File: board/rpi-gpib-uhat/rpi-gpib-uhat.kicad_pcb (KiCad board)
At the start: 2 copper layers, 65 x 30 mm, 44 parts, among them J1 RPI_GPIO, J2 GPIB, U1 SN75160BDW, U2 SN75162BDW, U3 LM317_SOT-223, U4 CAT24C32

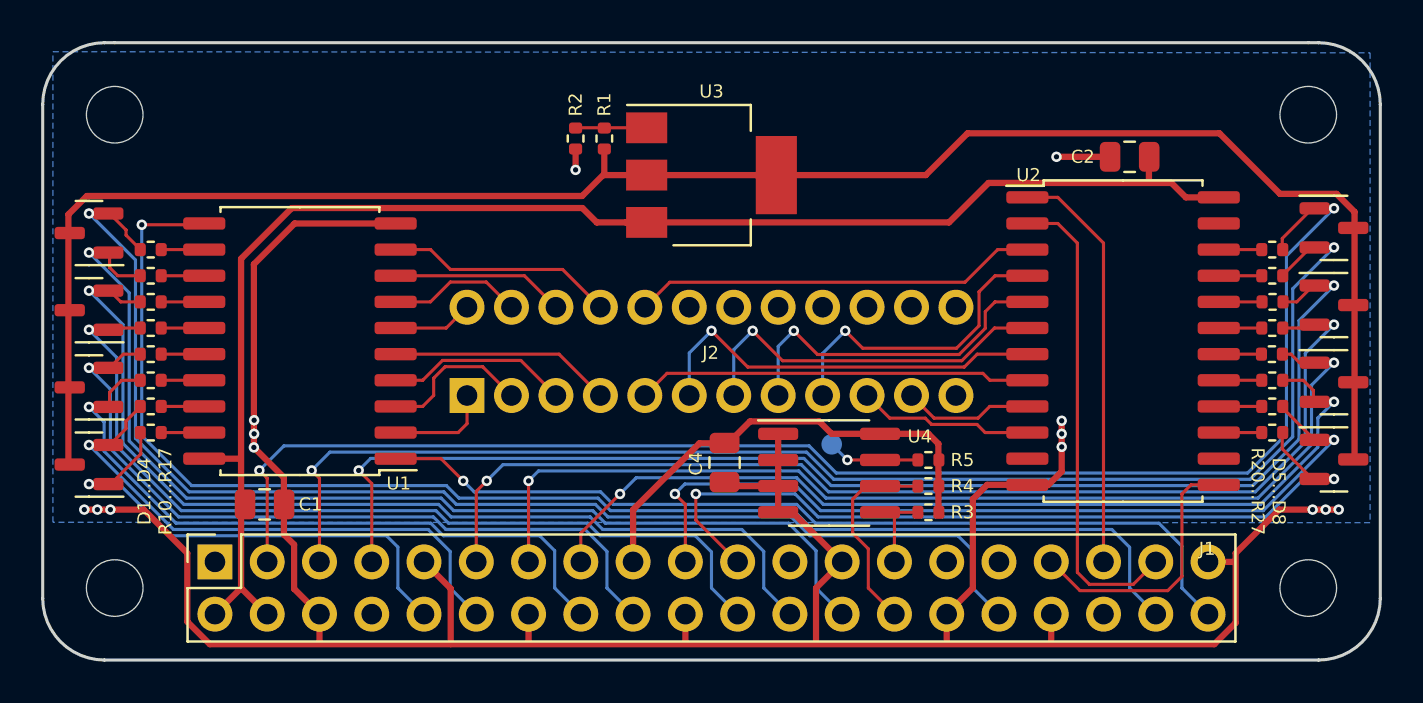
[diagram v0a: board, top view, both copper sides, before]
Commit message: Change uHAT pinout and re-route.
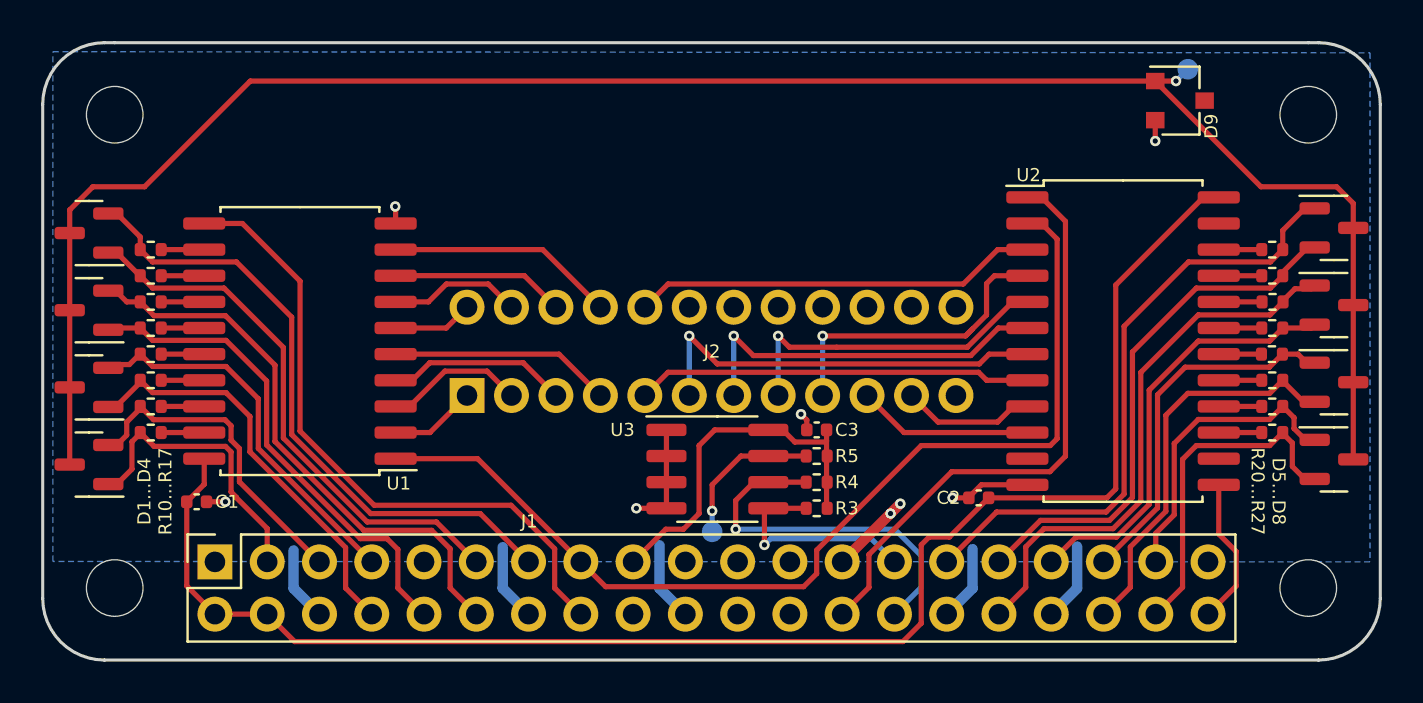
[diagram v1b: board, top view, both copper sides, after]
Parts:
- removed R1, R2: 100R, Resistor_SMD:R_0402_1005Metric
- removed the U3 at (129.0, 102.9)
- added D9: MMBZ5222BLT1G, Package_TO_SOT_SMD:SC-59, F.Cu at (151.8, 99.3)
- added TP2: TestPoint, TestPoint:TestPoint_Pad_D1.0mm, B.Cu at (152.1, 97.8)
- C1, C2: value 1u -> 100n; footprint Capacitor_SMD:C_0805_2012Metric -> Capacitor_SMD:C_0402_1005Metric
- C3: renamed from C4; value 1u -> 100n; footprint Capacitor_SMD:C_0805_2012Metric -> Capacitor_SMD:C_0402_1005Metric
- J1: value RPI_GPIO -> RasPi_Header_40W; footprint lib:PinSocket_2x20_P2.54mm_Vertical_Centered_Anchor -> local:PinSocket_2x20_P2.54mm_Vertical_Centered_Anchor
- J2: footprint local:NorComp_111-024-113L001 -> local:NorComp_111-024-113L001_NoScrews
- R10, R11, R12, R13, R14, R15, R16, R17, R20, R21, R22, R23, R24, R25, R26, R27: value 500R -> 1k
- moved C2 18.1 mm to (142.0, 118.6)
- moved TP1 7.20 mm to (129.0, 120.3), turned to 180 degrees
- moved R3 5.43 mm to (134.1, 119.1), turned to 0 degrees
- moved R4 5.43 mm to (134.1, 117.9), turned to 0 degrees
- moved R5 5.43 mm to (134.1, 116.6), turned to 0 degrees
- moved U3 5.43 mm to (129.3, 117.2)
- moved C3 4.75 mm to (134.1, 115.3), turned to 180 degrees
- moved C1 3.30 mm to (104.0, 118.8)
- renumbered U4 to U3
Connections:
- net /I_NDAC renamed /I_~{DAC}
- net /I_NRFD renamed /I_~{RFD}
- net /NDAC renamed /B_~{DAC}
- net /NRFD renamed /B_~{RFD}
- D1 pad 1: /GPIO15 -> /DIO1
- D1 pad 2: /GPIO18 -> /DIO2
- D2 pad 1: /GPIO23 -> /DIO3
- D2 pad 2: /GPIO24 -> /DIO4
- D3 pad 1: /GPIO25 -> /DIO5
- D3 pad 2: /GPIO8 -> /DIO6
- D4 pad 1: /GPIO7 -> /DIO7
- D4 pad 2: /GPIO12 -> /DIO8
- D5 pad 1: /GPIO2 -> /REN
- D5 pad 2: /GPIO3 -> /IFC
- D6 pad 1: /GPIO4 -> /~{DAC}
- D6 pad 2: /GPIO17 -> /~{RFD}
- D7 pad 1: /GPIO27 -> /DAV
- D7 pad 2: /GPIO22 -> /EOI
- D8 pad 1: /GPIO10 -> /ATN
- D8 pad 2: /GPIO9 -> /SRQ
- J1 pad 1: +3V3 -> unconnected-(J1-Pad1)
- J1 pad 10: /GPIO15 -> /DIO5
- J1 pad 11: /GPIO17 -> /DIO7
- J1 pad 12: /GPIO18 -> /DIO6
- J1 pad 13: /GPIO27 -> /DIO8
- J1 pad 15: /GPIO22 -> /TE
- J1 pad 16: /GPIO23 -> /~{PE}
- J1 pad 18: /GPIO24 -> unconnected-(J1-Pad18)
- J1 pad 19: /GPIO10 -> unconnected-(J1-Pad19)
- J1 pad 21: /GPIO9 -> unconnected-(J1-Pad21)
- J1 pad 22: /GPIO25 -> unconnected-(J1-Pad22)
- J1 pad 23: /GPIO11 -> unconnected-(J1-Pad23)
- J1 pad 24: /GPIO8 -> unconnected-(J1-Pad24)
- J1 pad 26: /GPIO7 -> /SC
- J1 pad 29: /GPIO5 -> /REN
- J1 pad 3: /GPIO2 -> /DIO1
- J1 pad 31: /GPIO6 -> /IFC
- J1 pad 32: /GPIO12 -> /~{DAC}
- J1 pad 33: /GPIO13 -> /~{RFD}
- J1 pad 35: /GPIO19 -> /DAV
- J1 pad 36: /GPIO16 -> /EOI
- J1 pad 37: /GPIO26 -> /ATN
- J1 pad 38: /GPIO20 -> /SRQ
- J1 pad 40: /GPIO21 -> /DC
- J1 pad 5: /GPIO3 -> /DIO2
- J1 pad 7: /GPIO4 -> /DIO4
- J1 pad 8: /GPIO14 -> /DIO3
- J2 pad 1: /DIO1 -> /B_DIO1
- J2 pad 10: /SRQ -> /B_SRQ
- J2 pad 11: /ATN -> /B_ATN
- J2 pad 12: Earth_Clean -> unconnected-(J2-Pad12)
- J2 pad 13: /DIO5 -> /B_DIO5
- J2 pad 14: /DIO6 -> /B_DIO6
- J2 pad 15: /DIO7 -> /B_DIO7
- J2 pad 16: /DIO8 -> /B_DIO8
- J2 pad 17: /REN -> /B_REN
- J2 pad 2: /DIO2 -> /B_DIO2
- J2 pad 3: /DIO3 -> /B_DIO3
- J2 pad 4: /DIO4 -> /B_DIO4
- J2 pad 5: /EOI -> /B_EOI
- J2 pad 6: /DAV -> /B_DAV
- J2 pad 9: /IFC -> /B_IFC
- R10 pad 2: /GPIO15 -> /DIO1
- R11 pad 2: /GPIO18 -> /DIO2
- R12 pad 2: /GPIO23 -> /DIO3
- R13 pad 2: /GPIO24 -> /DIO4
- R14 pad 2: /GPIO25 -> /DIO5
- R15 pad 2: /GPIO8 -> /DIO6
- R16 pad 2: /GPIO7 -> /DIO7
- R17 pad 2: /GPIO12 -> /DIO8
- R20 pad 2: /GPIO2 -> /REN
- R21 pad 2: /GPIO3 -> /IFC
- R22 pad 2: /GPIO4 -> /~{DAC}
- R23 pad 2: /GPIO17 -> /~{RFD}
- R24 pad 2: /GPIO27 -> /DAV
- R25 pad 2: /GPIO22 -> /EOI
- R26 pad 2: /GPIO10 -> /ATN
- R27 pad 2: /GPIO9 -> /SRQ
- R3 pad 1: +3V3 -> /ID_SD
- R3 pad 2: /ID_SD -> +3V3
- R4 pad 1: +3V3 -> /ID_SC
- R4 pad 2: /ID_SC -> +3V3
- R5 pad 1: +3V3 -> /ID_WP
- R5 pad 2: /ID_WP -> +3V3
- U1 pad 1: /GPIO21 -> /TE
- U1 pad 11: /GPIO20 -> /~{PE}
- U1 pad 2: /DIO1 -> /B_DIO1
- U1 pad 3: /DIO2 -> /B_DIO2
- U1 pad 4: /DIO3 -> /B_DIO3
- U1 pad 5: /DIO4 -> /B_DIO4
- U1 pad 6: /DIO5 -> /B_DIO5
- U1 pad 7: /DIO6 -> /B_DIO6
- U1 pad 8: /DIO7 -> /B_DIO7
- U1 pad 9: /DIO8 -> /B_DIO8
- U2 pad 1: /GPIO19 -> /SC
- U2 pad 10: /SRQ -> /B_SRQ
- U2 pad 13: /GPIO13 -> /DC
- U2 pad 2: /GPIO26 -> /TE
- U2 pad 3: /REN -> /B_REN
- U2 pad 4: /IFC -> /B_IFC
- U2 pad 7: /DAV -> /B_DAV
- U2 pad 8: /EOI -> /B_EOI
- U2 pad 9: /ATN -> /B_ATN
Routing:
- net GND: track 141.5 -> 35.6 mm, vias 14 -> 8
- net /GPIO2: track 71.9 -> 0.00 mm, vias 2 -> 0
- net /GPIO20: track 67.3 -> 0.00 mm, vias 1 -> 0
- net /GPIO3: track 67.2 -> 0.00 mm, vias 2 -> 0
- net /GPIO4: track 63.1 -> 0.00 mm, vias 2 -> 0
- net /GPIO12: track 61.8 -> 0.00 mm, vias 1 -> 0
- net /GPIO17: track 54.7 -> 0.00 mm, vias 2 -> 0
- net /GPIO7: track 52.6 -> 0.00 mm, vias 1 -> 0
- net /GPIO27: track 50.9 -> 0.00 mm, vias 2 -> 0
- net /TE: track 0.00 -> 49.8 mm
- net /GPIO8: track 47.7 -> 0.00 mm, vias 1 -> 0
- net /GPIO22: track 45.8 -> 0.00 mm, vias 2 -> 0
- net /GPIO21: track 43.8 -> 0.00 mm, vias 1 -> 0
- net /GPIO24: track 43.5 -> 0.00 mm, vias 1 -> 0
- net /GPIO25: track 43.3 -> 0.00 mm, vias 1 -> 0
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
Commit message: Add FET switch for bus drivers.
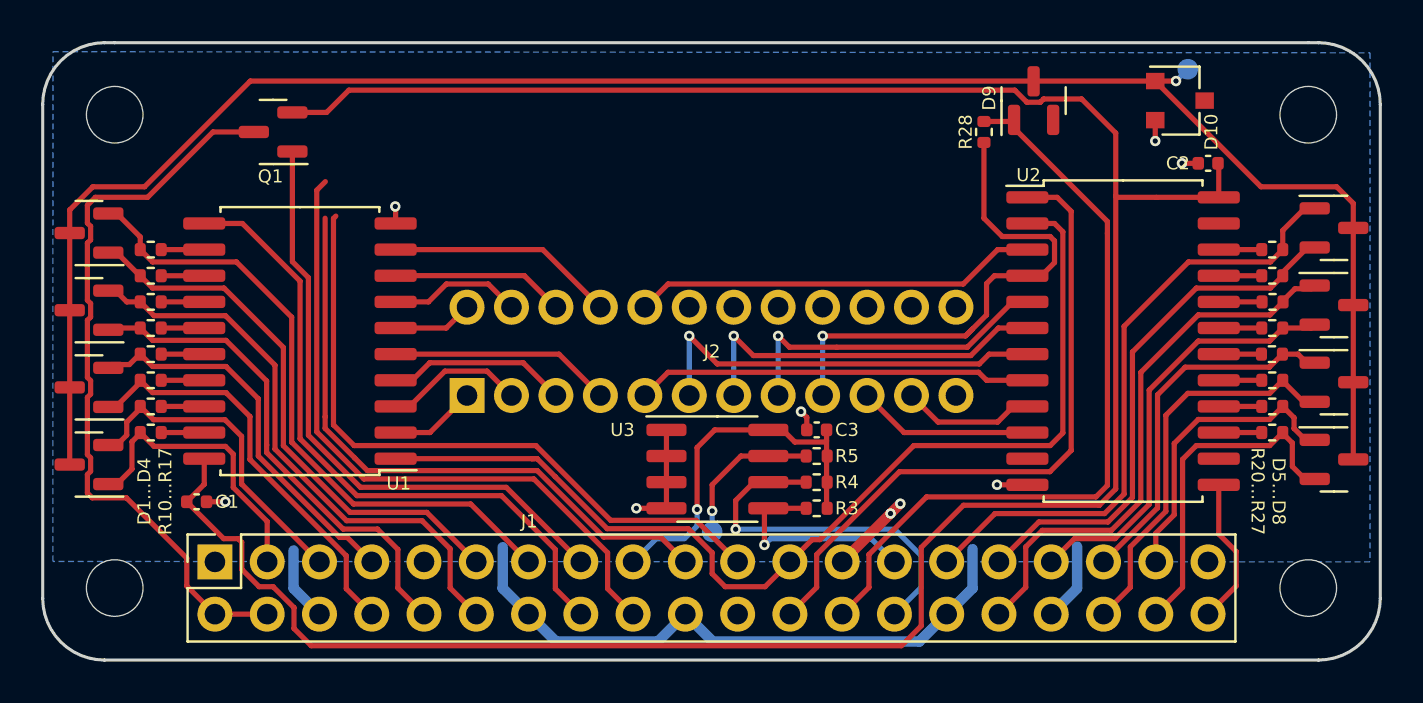
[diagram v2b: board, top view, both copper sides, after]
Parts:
- added D9: BAT54C, Package_TO_SOT_SMD:SOT-23, F.Cu at (144.7, 99.3)
- added Q1: BSH105, Package_TO_SOT_SMD:SOT-23, F.Cu at (107.7, 100.8)
- added R28: 1k, Resistor_SMD:R_0402_1005Metric, F.Cu at (142.2, 100.8)
- moved C2 19.7 mm to (153.1, 102.4)
- renumbered D9 to D10
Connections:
- C1 pad 1: +5V -> Net-(C1-Pad1)
- C2 pad 1: +5V -> Net-(C1-Pad1)
- J1 pad 15: /TE -> /ON_BUS
- J1 pad 23: unconnected-(J1-Pad23) -> /TE
- J1 pad 24: unconnected-(J1-Pad24) -> /SC
- J1 pad 26: /SC -> /IFC_DET
- U1 pad 20: +5V -> Net-(C1-Pad1)
- U2 pad 24: +5V -> Net-(C1-Pad1)
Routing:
- net Net-(C1-Pad1): track 0.00 -> 122.7 mm
- net +5V: track 74.8 -> 36.0 mm
- net /IFC_DET: track 0.00 -> 37.6 mm
- net unconnected-(J1-Pad21): track 0.00 -> 32.6 mm
- net unconnected-(J1-Pad18): track 0.00 -> 32.4 mm
- net unconnected-(J1-Pad19): track 0.00 -> 30.4 mm
- net /ON_BUS: track 0.00 -> 29.9 mm
- net GND: track 35.6 -> 52.7 mm, vias 8 -> 9
- net /B_IFC: track 15.4 -> 25.6 mm
- net /SC: track 28.7 -> 31.9 mm
- net /TE: track 49.8 -> 50.5 mm
- net +3V3: track 18.1 -> 18.4 mm, vias 0 -> 1
